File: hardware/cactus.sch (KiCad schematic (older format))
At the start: 20 parts, among them SW1 SW_Push, U1 WeMos_Battery_Shield, U2 WeMos_D1_mini, U3 74HC595, U4 Si7021_breakout

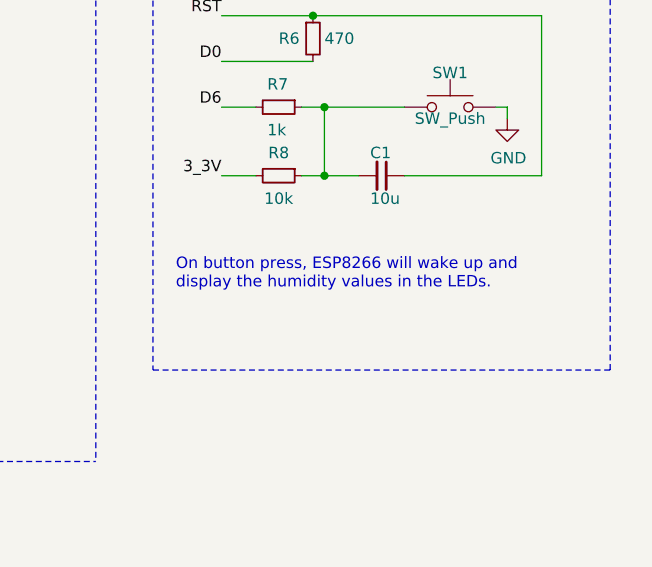
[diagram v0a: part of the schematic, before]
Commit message: [mech] Add note on long press button on silkscreen
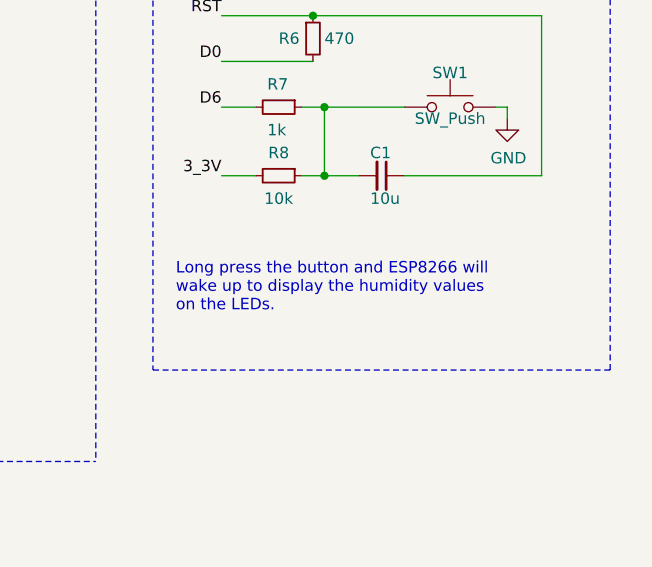
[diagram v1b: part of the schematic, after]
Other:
- note added: "Long press the button and ESP8266 will \nwake up to display the humidity values \non the LEDs."
- note removed: "On button press, ESP8266 will wake up and \ndisplay the humidity values in the LEDs."
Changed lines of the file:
@@
 Text Notes 900  3350 0    79   ~ 0
 Sensor circuit
-Text Notes 9000 2250 0    50   ~ 0
-On button press, ESP8266 will wake up and \ndisplay the humidity values in the LEDs.
+Text Notes 9000 2350 0    50   ~ 0
+Long press the button and ESP8266 will \nwake up to display the humidity values \non the LEDs.
 Text Notes 2150 1200 0    50   ~ 0
 WeMos Battery shield is \nconnected to a LiPo battery.
@@
 Data
 89 50 4E 47 0D 0A 1A 0A 00 00 00 0D 49 48 44 52 00 00 03 16 00 00 01 3B 08 02 00 00 00 CF 71 80
-31 00 00 00 03 73 42 49 54 08 08 08 DB E1 4F E0 00 00 00 09 70 48 59 73 00 00 0B 12 00 00 0B 12
-01 D2 DD 7E FC 00 00 20 00 49 44 41 54 78 9C EC BD 77 90 5D F7 75 E7 79 CE F9 85 7B EF 4B 1D D0
+31 00 00 00 03 73 42 49 54 08 08 08 DB E1 4F E0 00 00 00 09 70 48 59 73 00 00 0A F0 00 00 0A F0
+01 42 AC 34 98 00 00 20 00 49 44 41 54 78 9C EC BD 77 90 5D F7 75 E7 79 CE F9 85 7B EF 4B 1D D0
 68 44 12 04 01 30 80 60 A6 44 52 96 44 89 22 4D C9 4A 36 6D 39 CD D8 3B F6 1F BB B5 EB 5D 57 B9
 CA B5 B3 6B CF EE D8 35 3B F6 CE 78 CA BB F6 DA 9E B1 E5 72 92 AD 91 35 B2 9C 94 49 5B 94 68 E6
